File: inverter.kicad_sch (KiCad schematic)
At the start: 28 parts, among them Q1 IRF530NPBF, Q2 IRF530NPBF, Q3 IRF530NPBF, Q4 IRF530NPBF, U1 IR2110, U2 IR2110

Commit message: Autosave
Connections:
- net 12V: no longer U2.3 (VCC)
- net VCC_Inverter: now also U2.3 (VCC)
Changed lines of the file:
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@@
 	(wire
 		(pts
+			(xy 241.3 64.77) (xy 242.57 64.77)
+		)
+		(stroke
+			(width 0)
+			(type default)
+		)
+	)
+	(wire
+		(pts
 			(xy 64.77 62.23) (xy 74.93 62.23)
 		)
@@
 	(wire
 		(pts
-			(xy 242.57 64.77) (xy 238.76 64.77)
-		)
-		(stroke
-			(width 0)
-			(type default)
-		)
-	)
-	(wire
-		(pts
 			(xy 77.47 46.99) (xy 77.47 39.37)
 		)
@@
 	)
 	(label "VCC_Inverter"
+		(at 241.3 64.77 180)
+		(effects
+			(font
+				(size 1.27 1.27)
+			)
+			(justify right bottom)
+		)
+	)
+	(label "VCC_Inverter"
 		(at 54.61 27.94 0)
 		(effects
@@
 					(unit 1)
 				)
-			)
-		)
-	)
-	(symbol
-		(lib_id "power:VCC")
-		(at 238.76 64.77 90)
-		(mirror x)
-		(unit 1)
-		(body_style 1)
-		(exclude_from_sim no)
-		(in_bom yes)
-		(on_board yes)
-		(in_pos_files yes)
-		(dnp no)
-		(fields_autoplaced yes)
-		(property "Reference" "#PWR011"
-			(at 242.57 64.77 0)
-			(hide yes)
-			(show_name no)
-			(do_not_autoplace no)
-			(effects
-				(font
-					(size 1.27 1.27)
-				)
-			)
-		)
-		(property "Value" "12V"
-			(at 234.95 64.7699 90)
-			(show_name no)
-			(do_not_autoplace no)
-			(effects
-				(font
-					(size 1.27 1.27)
-				)
-				(justify left)
-			)
-		)
-		(property "Footprint" ""
-			(at 238.76 64.77 0)
-			(hide yes)
-			(show_name no)
-			(do_not_autoplace no)
-			(effects
-				(font
-					(size 1.27 1.27)
-				)
-			)
-		)
-		(property "Datasheet" ""
-			(at 238.76 64.77 0)
-			(hide yes)
-			(show_name no)
-			(do_not_autoplace no)
-			(effects
-				(font
-					(size 1.27 1.27)
-				)
-			)
-		)
-		(property "Description" "Power symbol creates a global label with name \"VCC\""
-			(at 238.76 64.77 0)
-			(hide yes)
-			(show_name no)
-			(do_not_autoplace no)
-			(effects
-				(font
-					(size 1.27 1.27)
-				)
-			)
-		)
-		(pin "1"
-		)
-		(instances
-			(project "WET_PCB_v2"
-				(path "/13451c35-1666-47d9-9525-8d8125ba1cf3/a035cbd1-b4bf-441e-99d9-9f1401ee5bfe"
-					(reference "#PWR011")
-					(unit 1)
-				)

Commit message: SCH Save: 2 files changed inverter.kicad_sch 268/0/102 WET_PCB_v2.kicad_pro 54/0/1
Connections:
- net VCC_Inverter is gone; now on net 12V: D1.2 (A), U1.3 (VCC), U2.3 (VCC)
- net VDD_Inverter is gone; now on net 5V: C1.2, U1.9 (VDD)
- net Inv_Driver_Left_Hin: no longer names the net of U1.10 (HIN)
- net Inv_Driver_Left_Lin: no longer names the net of U1.12 (LIN)
- net Inv_Driver_Left_SD: no longer names the net of U1.11 (SD)
- net Inv_Driver_Right_Hin renamed Hin
- net Inv_Driver_Right_Lin renamed Lin
- net Inv_Driver_Right_SD renamed Off

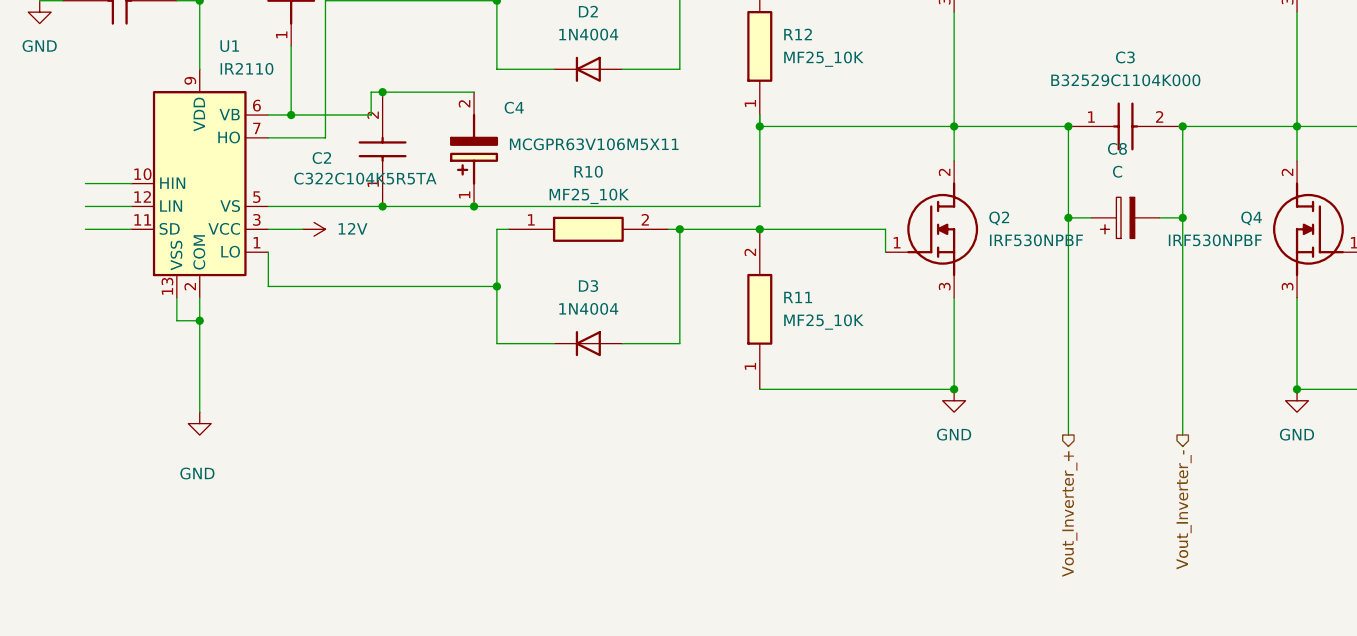
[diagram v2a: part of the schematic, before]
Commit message: SCH Save: 2 files changed GateDriver.kicad_sch 0/0/4 inverter.kicad_sch 28/0/10
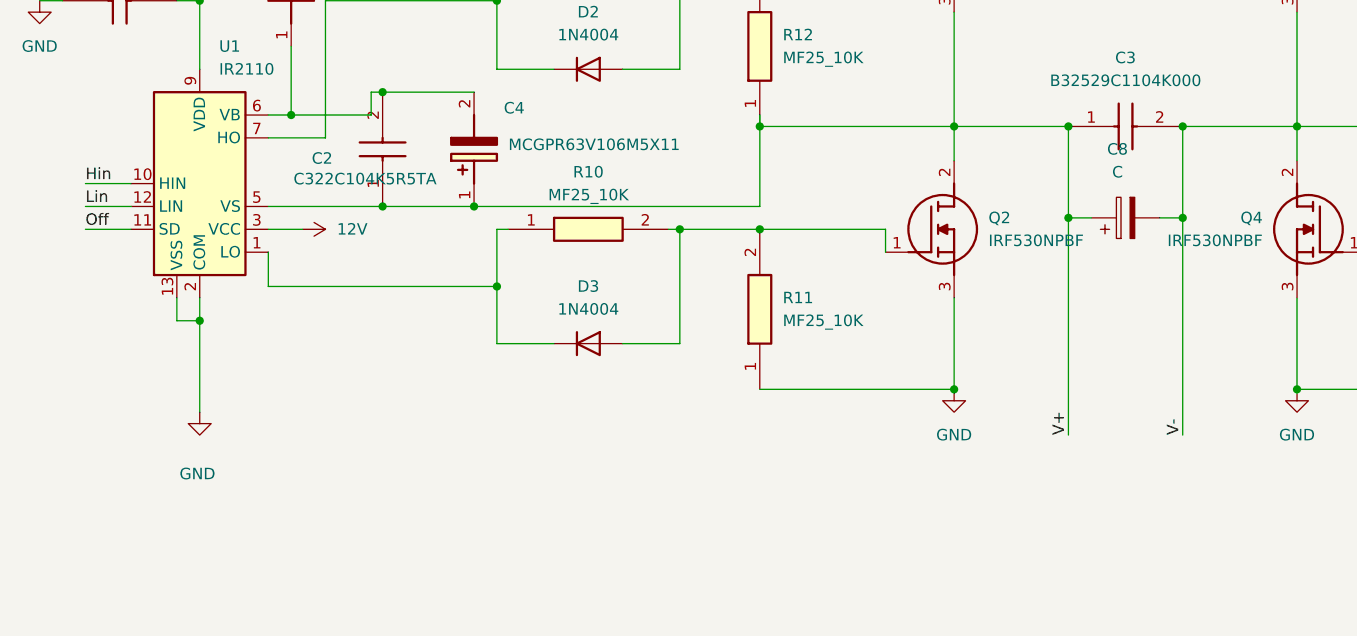
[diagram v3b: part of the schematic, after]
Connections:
- net Hin: now also U1.10 (HIN)
- net Lin: now also U1.12 (LIN)
- net Off: now also U1.11 (SD)
- net Vout_Inverter_+ renamed V+
- net Vout_Inverter_- renamed V-
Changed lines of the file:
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@@
+	)
+	(label "Hin"
+		(at 31.75 59.69 0)
+		(effects
+			(font
+				(size 1.27 1.27)
+			)
+			(justify left bottom)
+		)
+	)
+	(label "Lin"
+		(at 31.75 62.23 0)
+		(effects
+			(font
+				(size 1.27 1.27)
+			)
+			(justify left bottom)
+		)
+	)
+	(label "V+"
+		(at 140.97 87.63 90)
+		(effects
+			(font
+				(size 1.27 1.27)
+			)
+			(justify left bottom)
+		)
 	)
 	(label "Hin"
@@
 		)
 	)
-	(hierarchical_label "Vout_Inverter_-"
-		(shape output)
-		(at 153.67 87.63 270)
+	(label "V-"
+		(at 153.67 87.63 90)
 		(effects
 			(font
 				(size 1.27 1.27)
 			)
-			(justify right)
+			(justify left bottom)
 		)
 	)
-	(hierarchical_label "Vout_Inverter_+"
-		(shape output)
-		(at 140.97 87.63 270)
+	(label "Off"
+		(at 31.75 64.77 0)
 		(effects
 			(font
 				(size 1.27 1.27)
 			)
-			(justify right)
+			(justify left bottom)
 		)
 	)

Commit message: SCH Save: 1 files changed inverter.kicad_sch 0/28/10
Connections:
- net Hin: no longer U1.10 (HIN)
- net Lin: no longer U1.12 (LIN)
- net Off: no longer U1.11 (SD)
- net V+ renamed Vout_Inverter_+
- net V- renamed Vout_Inverter_-
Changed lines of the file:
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@@
-	)
-	(label "Hin"
-		(at 31.75 59.69 0)
-		(effects
-			(font
-				(size 1.27 1.27)
-			)
-			(justify left bottom)
-		)
-	)
-	(label "Lin"
-		(at 31.75 62.23 0)
-		(effects
-			(font
-				(size 1.27 1.27)
-			)
-			(justify left bottom)
-		)
-	)
-	(label "V+"
-		(at 140.97 87.63 90)
-		(effects
-			(font
-				(size 1.27 1.27)
-			)
-			(justify left bottom)
-		)
 	)
 	(label "Hin"
@@
 		)
 	)
-	(label "V-"
-		(at 153.67 87.63 90)
+	(hierarchical_label "Vout_Inverter_-"
+		(shape output)
+		(at 153.67 87.63 270)
 		(effects
 			(font
 				(size 1.27 1.27)
 			)
-			(justify left bottom)
+			(justify right)
 		)
 	)
-	(label "Off"
-		(at 31.75 64.77 0)
+	(hierarchical_label "Vout_Inverter_+"
+		(shape output)
+		(at 140.97 87.63 270)
 		(effects
 			(font
 				(size 1.27 1.27)
 			)
-			(justify left bottom)
+			(justify right)
 		)
 	)

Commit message: SCH Save: 1 files changed inverter.kicad_sch 0/268/102
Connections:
- net 12V: no longer D1.2 (A), U1.3 (VCC), U2.3 (VCC)
- net 5V: no longer C1.2, U1.9 (VDD)
- net Inv_Driver_Left_Hin: now reaches U1.10 (HIN)
- net Inv_Driver_Left_SD: now reaches U1.11 (SD)
- net Inv_Driver_Left_Lin: now reaches U1.12 (LIN)
- net Hin renamed Inv_Driver_Right_Hin
- net Lin renamed Inv_Driver_Right_Lin
- net Off renamed Inv_Driver_Right_SD
- new net VCC_Inverter: D1.2 (A), U1.3 (VCC), U2.3 (VCC)
- new net VDD_Inverter: C1.2, U1.9 (VDD)

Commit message: Autosave
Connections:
- net 12V is gone; now on net VCC_Inverter: D4.2 (A)
- net 5V: no longer names the net of C5.2, U2.9 (VDD)
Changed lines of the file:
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@@
 	)
 	(label "VCC_Inverter"
+		(at 240.03 25.4 180)
+		(effects
+			(font
+				(size 1.27 1.27)
+			)
+			(justify right bottom)
+		)
+	)
+	(label "VCC_Inverter"
 		(at 54.61 27.94 0)
 		(effects
@@
 	)
 	(symbol
-		(lib_id "power:VCC")
-		(at 240.03 25.4 0)
-		(mirror y)
-		(unit 1)
-		(body_style 1)
-		(exclude_from_sim no)
-		(in_bom yes)
-		(on_board yes)
-		(in_pos_files yes)
-		(dnp no)
-		(fields_autoplaced yes)
-		(property "Reference" "#PWR010"
-			(at 240.03 29.21 0)
-			(hide yes)
-			(show_name no)
-			(do_not_autoplace no)
-			(effects
-				(font
-					(size 1.27 1.27)
-				)
-			)
-		)
-		(property "Value" "12V"
-			(at 240.03 20.32 0)
-			(show_name no)
-			(do_not_autoplace no)
-			(effects
-				(font
-					(size 1.27 1.27)
-				)
-			)
-		)
-		(property "Footprint" ""
-			(at 240.03 25.4 0)
-			(hide yes)
-			(show_name no)
-			(do_not_autoplace no)
-			(effects
-				(font
-					(size 1.27 1.27)
-				)
-			)
-		)
-		(property "Datasheet" ""
-			(at 240.03 25.4 0)
-			(hide yes)
-			(show_name no)
-			(do_not_autoplace no)
-			(effects
-				(font
-					(size 1.27 1.27)
-				)
-			)
-		)
-		(property "Description" "Power symbol creates a global label with name \"VCC\""
-			(at 240.03 25.4 0)
-			(hide yes)
-			(show_name no)
-			(do_not_autoplace no)
-			(effects
-				(font
-					(size 1.27 1.27)
-				)
-			)
-		)
-		(pin "1"
-		)
-		(instances
-			(project "WET_PCB_v2"
-				(path "/13451c35-1666-47d9-9525-8d8125ba1cf3/a035cbd1-b4bf-441e-99d9-9f1401ee5bfe"
-					(reference "#PWR010")
-					(unit 1)
-				)
-			)
-		)
-	)
-	(symbol
 		(lib_id "power:GND")
 		(at 166.37 82.55 0)
@@
 					(unit 1)
 				)
-			)
-		)
-	)
-	(symbol
-		(lib_id "power:VCC")
-		(at 250.19 25.4 0)
-		(mirror y)
-		(unit 1)
-		(body_style 1)
-		(exclude_from_sim no)
-		(in_bom yes)
-		(on_board yes)
-		(in_pos_files yes)
-		(dnp no)
-		(fields_autoplaced yes)
-		(property "Reference" "#PWR08"
-			(at 250.19 29.21 0)
-			(hide yes)
-			(show_name no)
-			(do_not_autoplace no)
-			(effects
-				(font
-					(size 1.27 1.27)
-				)
-			)
-		)
-		(property "Value" "5V"
-			(at 250.19 20.32 0)
-			(show_name no)
-			(do_not_autoplace no)
-			(effects
-				(font
-					(size 1.27 1.27)
-				)
-			)
-		)
-		(property "Footprint" ""
-			(at 250.19 25.4 0)
-			(hide yes)
-			(show_name no)
-			(do_not_autoplace no)
-			(effects
-				(font
-					(size 1.27 1.27)
-				)
-			)
-		)
-		(property "Datasheet" ""
-			(at 250.19 25.4 0)
-			(hide yes)
-			(show_name no)
-			(do_not_autoplace no)
-			(effects
-				(font
-					(size 1.27 1.27)
-				)
-			)
-		)
-		(property "Description" "Power symbol creates a global label with name \"VCC\""
-			(at 250.19 25.4 0)
-			(hide yes)
-			(show_name no)
-			(do_not_autoplace no)
-			(effects
-				(font
-					(size 1.27 1.27)
-				)
-			)
-		)
-		(pin "1"
-		)
-		(instances
-			(project "WET_PCB_v2"
-				(path "/13451c35-1666-47d9-9525-8d8125ba1cf3/a035cbd1-b4bf-441e-99d9-9f1401ee5bfe"
-					(reference "#PWR08")
-					(unit 1)
-				)

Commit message: Autosave
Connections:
- net VDD_Inverter: now also C5.2, U2.9 (VDD)
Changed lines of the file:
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@@
 	(wire
 		(pts
-			(xy 54.61 27.94) (xy 54.61 29.21)
+			(xy 54.61 25.4) (xy 54.61 29.21)
 		)
 		(stroke
@@
 		)
 	)
-	(label "VCC_Inverter"
-		(at 54.61 27.94 0)
+	(label "VDD_Inverter"
+		(at 250.19 25.4 0)
 		(effects
 			(font
@@
 		)
 	)
+	(label "VCC_Inverter"
+		(at 54.61 25.4 0)
+		(effects
+			(font
+				(size 1.27 1.27)
+			)
+			(justify left bottom)
+		)
+	)
 	(label "VDD_Inverter"
-		(at 44.45 25.4 0)
-		(effects
-			(font
-				(size 1.27 1.27)
-			)
-			(justify left bottom)
-		)
-	)
+		(at 44.45 25.4 180)
+		(effects
+			(font
+				(size 1.27 1.27)
+			)
+			(justify right bottom)
+		)
+	)
